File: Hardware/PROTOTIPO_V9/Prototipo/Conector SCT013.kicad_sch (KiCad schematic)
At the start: 3 parts, among them J6 Conn_01x01, J7 Conn_01x01, J8 Conn_01x01

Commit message: Asignación de huellas
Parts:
- J6, J7, J8: footprint (none) -> Connector_PinHeader_2.54mm:PinHeader_1x01_P2.54mm_Vertical
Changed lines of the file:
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@@
 			)
 		)
-		(property "Footprint" ""
+		(property "Footprint" "Connector_PinHeader_2.54mm:PinHeader_1x01_P2.54mm_Vertical"
 			(at 148.59 82.55 0)
 			(effects
@@
 			)
 		)
-		(property "Footprint" ""
+		(property "Footprint" "Connector_PinHeader_2.54mm:PinHeader_1x01_P2.54mm_Vertical"
 			(at 142.24 88.9 0)
 			(effects
@@
 			)
 		)
-		(property "Footprint" ""
+		(property "Footprint" "Connector_PinHeader_2.54mm:PinHeader_1x01_P2.54mm_Vertical"
 			(at 148.59 95.25 0)
 			(effects

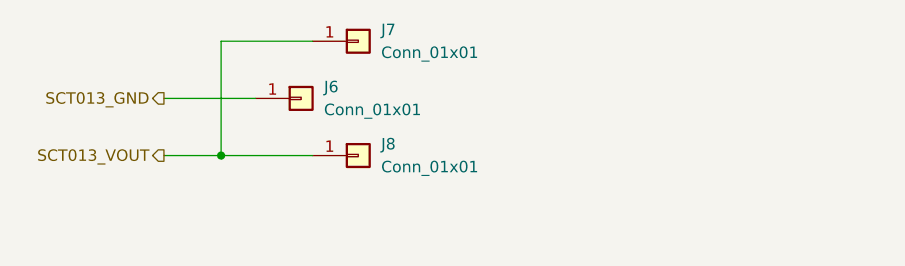
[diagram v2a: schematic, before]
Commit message: Esquematico TR de Corriente
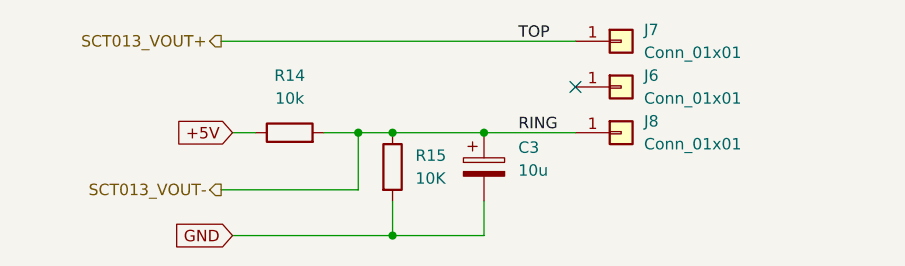
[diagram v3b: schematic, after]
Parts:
- added C3: 10u, symbol Device:C_Polarized
- added R14: 10k, symbol Device:R
- added R15: 10K, symbol Device:R
- J6, J7, J8: footprint Connector_PinHeader_2.54mm:PinHeader_1x01_P2.54mm_Vertical -> (none)
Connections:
- net SCT013_GND: no longer names the net of J6.1 (Pin_1)
- net SCT013_VOUT renamed SCT013_VOUT+
- net SCT013_VOUT+: no longer J8.1 (Pin_1)
- new net +5V: R14.1
- new net GND: C3.2, R15.2
- new net SCT013_VOUT-: C3.1, J8.1 (Pin_1), R14.2, R15.1
- no-connect marks 0 -> 1

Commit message: Esquematico completo v1.0
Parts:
- added R16: 100, symbol Device:R
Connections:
- net SCT013_VOUT+: now also R16.1
- net SCT013_VOUT-: now also R16.2
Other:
- moved on the sheet: J6, J7, J8
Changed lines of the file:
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@@
 		(color 0 0 0 0)
 	)
+	(junction
+		(at 177.8 92.71)
+		(diameter 0)
+		(color 0 0 0 0)
+	)
+	(junction
+		(at 177.8 82.55)
+		(diameter 0)
+		(color 0 0 0 0)
+	)
 	(no_connect
-		(at 172.72 87.63)
+		(at 186.69 87.63)
 	)
 	(wire
@@
 	(wire
 		(pts
+			(xy 177.8 83.82) (xy 177.8 82.55)
+		)
+		(stroke
+			(width 0)
+			(type default)
+		)
+	)
+	(wire
+		(pts
+			(xy 177.8 92.71) (xy 186.69 92.71)
+		)
+		(stroke
+			(width 0)
+			(type default)
+		)
+	)
+	(wire
+		(pts
+			(xy 177.8 91.44) (xy 177.8 92.71)
+		)
+		(stroke
+			(width 0)
+			(type default)
+		)
+	)
+	(wire
+		(pts
 			(xy 134.62 92.71) (xy 137.16 92.71)
 		)
@@
 	(wire
 		(pts
-			(xy 133.35 82.55) (xy 172.72 82.55)
+			(xy 133.35 82.55) (xy 177.8 82.55)
 		)
 		(stroke
@@
 	(wire
 		(pts
-			(xy 162.56 92.71) (xy 172.72 92.71)
+			(xy 162.56 92.71) (xy 177.8 92.71)
 		)
 		(stroke
@@
 		(pts
 			(xy 152.4 92.71) (xy 162.56 92.71)
+		)
+		(stroke
+			(width 0)
+			(type default)
+		)
+	)
+	(wire
+		(pts
+			(xy 177.8 82.55) (xy 186.69 82.55)
 		)
 		(stroke
@@
 	(symbol
 		(lib_id "Connector_Generic:Conn_01x01")
-		(at 177.8 92.71 0)
+		(at 191.77 92.71 0)
 		(unit 1)
 		(exclude_from_sim no)
@@
 		(fields_autoplaced yes)
 		(property "Reference" "J8"
-			(at 180.34 91.4399 0)
+			(at 194.31 91.4399 0)
 			(effects
 				(font
@@
 		)
 		(property "Value" "Conn_01x01"
-			(at 180.34 93.9799 0)
+			(at 194.31 93.9799 0)
 			(effects
 				(font
@@
 		)
 		(property "Footprint" ""
-			(at 177.8 92.71 0)
+			(at 191.77 92.71 0)
 			(effects
 				(font
@@
 		)
 		(property "Datasheet" "~"
-			(at 177.8 92.71 0)
+			(at 191.77 92.71 0)
 			(effects
 				(font
@@
 		)
 		(property "Description" "Generic connector, single row, 01x01, script generated (kicad-library-utils/schlib/autogen/connector/)"
-			(at 177.8 92.71 0)
+			(at 191.77 92.71 0)
 			(effects
 				(font
@@
 	(symbol
 		(lib_id "Connector_Generic:Conn_01x01")
-		(at 177.8 82.55 0)
+		(at 191.77 82.55 0)
 		(unit 1)
 		(exclude_from_sim no)
@@
 		(fields_autoplaced yes)
 		(property "Reference" "J7"
-			(at 180.34 81.2799 0)
+			(at 194.31 81.2799 0)
 			(effects
 				(font
@@
 		)
 		(property "Value" "Conn_01x01"
-			(at 180.34 83.8199 0)
+			(at 194.31 83.8199 0)
 			(effects
 				(font
@@
 		)
 		(property "Footprint" ""
-			(at 177.8 82.55 0)
+			(at 191.77 82.55 0)
 			(effects
 				(font
@@
 		)
 		(property "Datasheet" "~"
-			(at 177.8 82.55 0)
+			(at 191.77 82.55 0)
 			(effects
 				(font
@@
 		)
 		(property "Description" "Generic connector, single row, 01x01, script generated (kicad-library-utils/schlib/autogen/connector/)"
-			(at 177.8 82.55 0)
+			(at 191.77 82.55 0)
 			(effects
 				(font
@@
 	(symbol
 		(lib_id "Connector_Generic:Conn_01x01")
-		(at 177.8 87.63 0)
+		(at 191.77 87.63 0)
 		(unit 1)
 		(exclude_from_sim no)
@@
 		(fields_autoplaced yes)
 		(property "Reference" "J6"
-			(at 180.34 86.3599 0)
+			(at 194.31 86.3599 0)
 			(effects
 				(font
@@
 		)
 		(property "Value" "Conn_01x01"
-			(at 180.34 88.8999 0)
+			(at 194.31 88.8999 0)
 			(effects
 				(font
@@
 		)
 		(property "Footprint" ""
-			(at 177.8 87.63 0)
+			(at 191.77 87.63 0)
 			(effects
 				(font
@@
 		)
 		(property "Datasheet" "~"
-			(at 177.8 87.63 0)
+			(at 191.77 87.63 0)
 			(effects
 				(font
@@
 		)
 		(property "Description" "Generic connector, single row, 01x01, script generated (kicad-library-utils/schlib/autogen/connector/)"
-			(at 177.8 87.63 0)
+			(at 191.77 87.63 0)
 			(effects
 				(font
@@
 					(unit 1)
 				)
+			)
+		)
+	)
+	(symbol
+		(lib_id "Device:R")
+		(at 177.8 87.63 0)
+		(unit 1)
+		(exclude_from_sim no)
+		(in_bom yes)
+		(on_board yes)
+		(dnp no)
+		(fields_autoplaced yes)
+		(property "Reference" "R16"
+			(at 180.34 86.3599 0)
+			(effects
+				(font
+					(size 1.27 1.27)
+				)
+				(justify left)
+			)
+		)
+		(property "Value" "100"
+			(at 180.34 88.8999 0)
+			(effects
+				(font
+					(size 1.27 1.27)
+				)
+				(justify left)
+			)
+		)
+		(property "Footprint" ""
+			(at 176.022 87.63 90)
+			(effects
+				(font
+					(size 1.27 1.27)
+				)
+				(hide yes)
+			)
+		)
+		(property "Datasheet" "~"
+			(at 177.8 87.63 0)
+			(effects
+				(font
+					(size 1.27 1.27)
+				)
+				(hide yes)
+			)
+		)
+		(property "Description" "Resistor"
+			(at 177.8 87.63 0)
+			(effects
+				(font
+					(size 1.27 1.27)
+				)
+				(hide yes)
+			)
+		)
+		(pin "2"
+		)
+		(pin "1"
+		)
+		(instances
+			(project "Prototipo"
+				(path "/f7e5c6e4-37d6-479e-ad19-5d06867b62e9/671bd778-e511-4534-b337-b2c149ed4da7"
+					(reference "R16")
+					(unit 1)
+				)

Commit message: Footprints asignados
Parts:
- C3: footprint (none) -> Capacitor_THT:CP_Radial_D5.0mm_P2.50mm
- J6, J7, J8: footprint (none) -> Connector_PinSocket_2.54mm:PinSocket_1x01_P2.54mm_Horizontal
- R14, R15, R16: footprint (none) -> Resistor_THT:R_Axial_DIN0207_L6.3mm_D2.5mm_P10.16mm_Horizontal
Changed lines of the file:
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@@
 			)
 		)
-		(property "Footprint" ""
+		(property "Footprint" "Connector_PinSocket_2.54mm:PinSocket_1x01_P2.54mm_Horizontal"
 			(at 191.77 92.71 0)
 			(effects
@@
 			)
 		)
-		(property "Footprint" ""
+		(property "Footprint" "Resistor_THT:R_Axial_DIN0207_L6.3mm_D2.5mm_P10.16mm_Horizontal"
 			(at 140.97 94.488 90)
 			(effects
@@
 			)
 		)
-		(property "Footprint" ""
+		(property "Footprint" "Connector_PinSocket_2.54mm:PinSocket_1x01_P2.54mm_Horizontal"
 			(at 191.77 82.55 0)
 			(effects
@@
 			)
 		)
-		(property "Footprint" ""
+		(property "Footprint" "Connector_PinSocket_2.54mm:PinSocket_1x01_P2.54mm_Horizontal"
 			(at 191.77 87.63 0)
 			(effects
@@
 			)
 		)
-		(property "Footprint" ""
+		(property "Footprint" "Capacitor_THT:CP_Radial_D5.0mm_P2.50mm"
 			(at 163.5252 100.33 0)
 			(effects
@@
 			)
 		)
-		(property "Footprint" ""
+		(property "Footprint" "Resistor_THT:R_Axial_DIN0207_L6.3mm_D2.5mm_P10.16mm_Horizontal"
 			(at 176.022 87.63 90)
 			(effects
@@
 			)
 		)
-		(property "Footprint" ""
+		(property "Footprint" "Resistor_THT:R_Axial_DIN0207_L6.3mm_D2.5mm_P10.16mm_Horizontal"
 			(at 150.622 96.52 90)
 			(effects

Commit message: fp definitivos - Planteo de PCB con componentes
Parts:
- J6, J7, J8: footprint Connector_PinSocket_2.54mm:PinSocket_1x01_P2.54mm_Horizontal -> Connector_PinHeader_2.54mm:PinHeader_1x01_P2.54mm_Vertical
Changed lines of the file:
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@@
 			)
 		)
-		(property "Footprint" "Connector_PinSocket_2.54mm:PinSocket_1x01_P2.54mm_Horizontal"
+		(property "Footprint" "Connector_PinHeader_2.54mm:PinHeader_1x01_P2.54mm_Vertical"
 			(at 191.77 92.71 0)
 			(effects
@@
 			)
 		)
-		(property "Footprint" "Connector_PinSocket_2.54mm:PinSocket_1x01_P2.54mm_Horizontal"
+		(property "Footprint" "Connector_PinHeader_2.54mm:PinHeader_1x01_P2.54mm_Vertical"
 			(at 191.77 82.55 0)
 			(effects
@@
 			)
 		)
-		(property "Footprint" "Connector_PinSocket_2.54mm:PinSocket_1x01_P2.54mm_Horizontal"
+		(property "Footprint" "Connector_PinHeader_2.54mm:PinHeader_1x01_P2.54mm_Vertical"
 			(at 191.77 87.63 0)
 			(effects

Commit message: Migración de sch a BlackPill
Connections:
- net +5V renamed +3V3
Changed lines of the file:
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@@
 		)
 	)
-	(global_label "+5V"
+	(global_label "+3V3"
 		(shape input)
 		(at 134.62 92.71 180)
@@
 		)
 		(property "Intersheetrefs" "${INTERSHEET_REFS}"
-			(at 127.7643 92.71 0)
+			(at 126.5548 92.71 0)
 			(effects
 				(font
